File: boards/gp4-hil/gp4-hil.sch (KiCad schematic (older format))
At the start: 8 parts

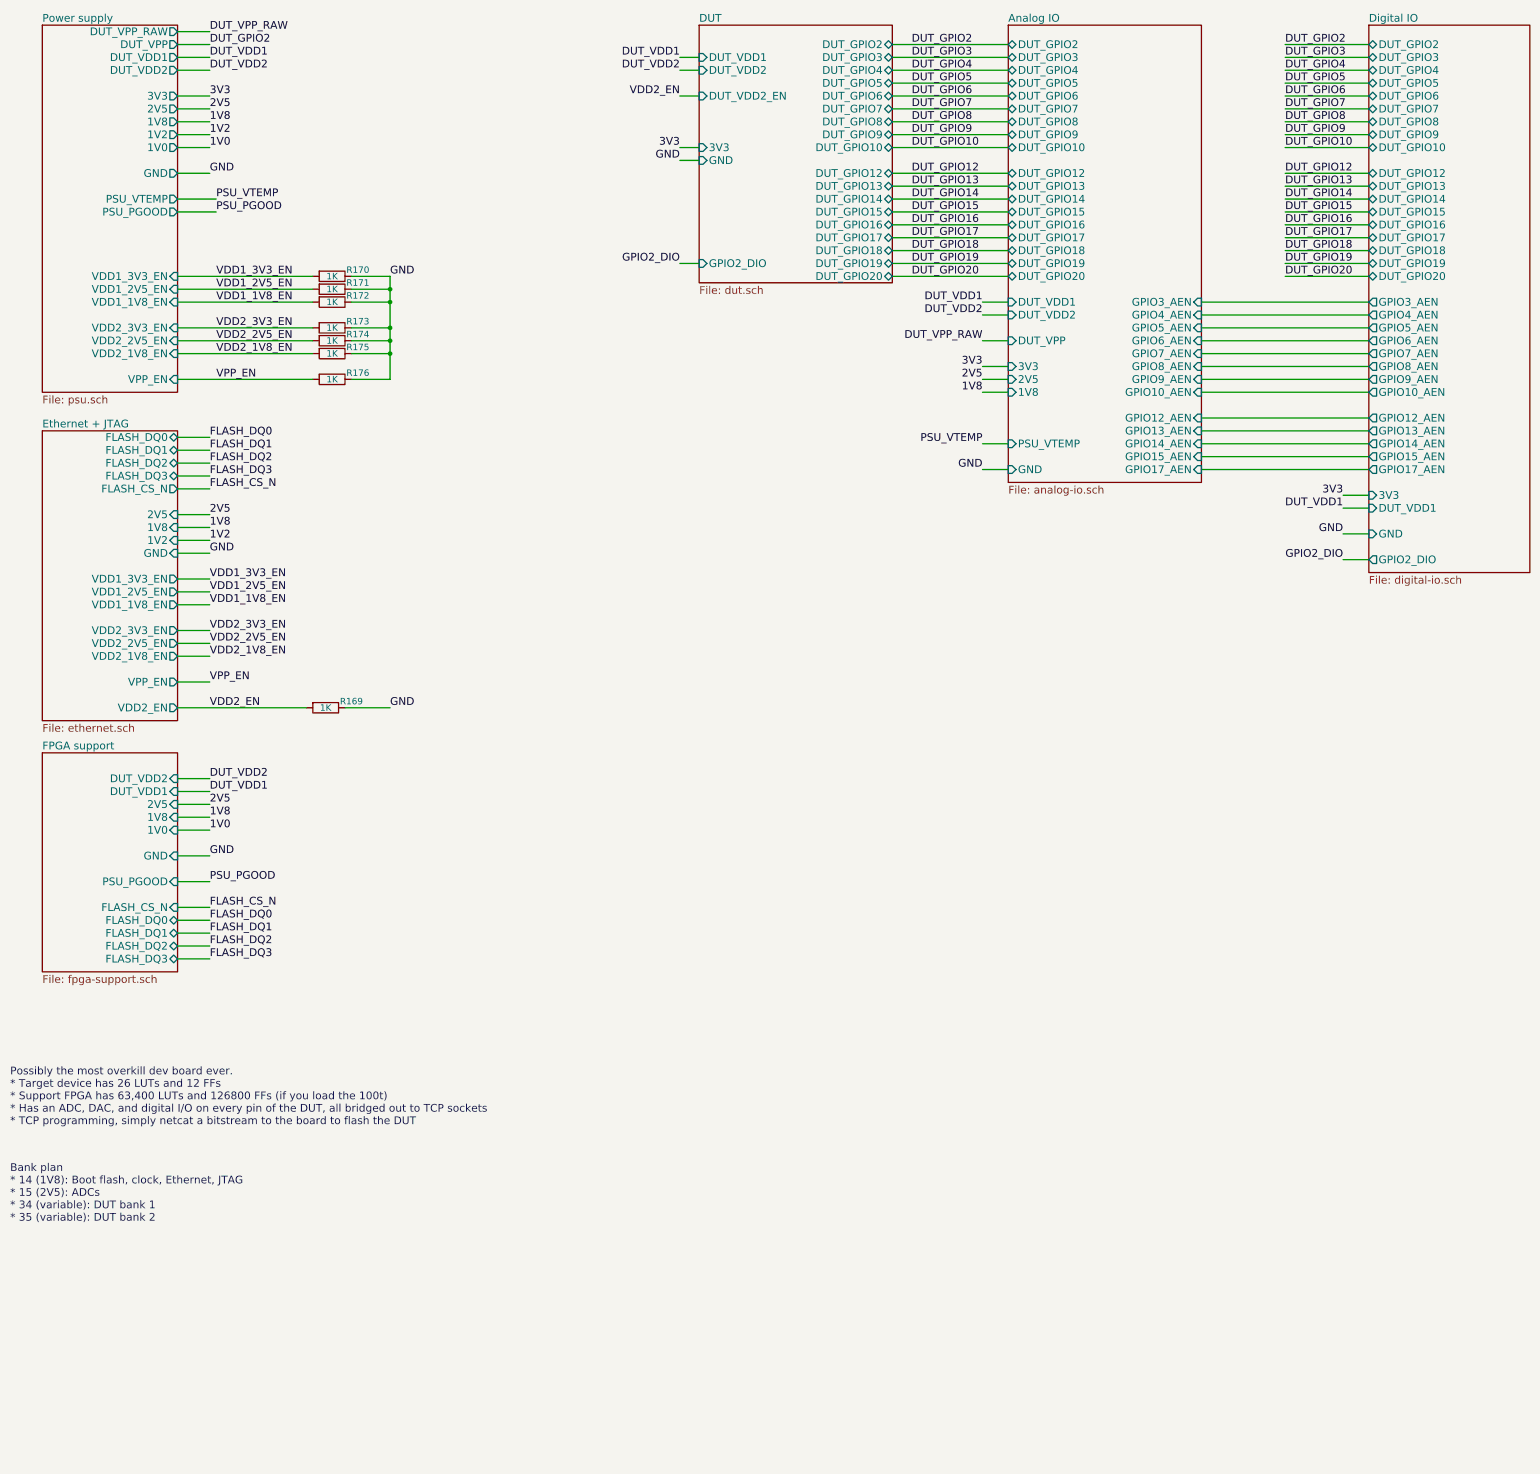
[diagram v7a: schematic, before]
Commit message: Added current monitoring shunts. Began design review
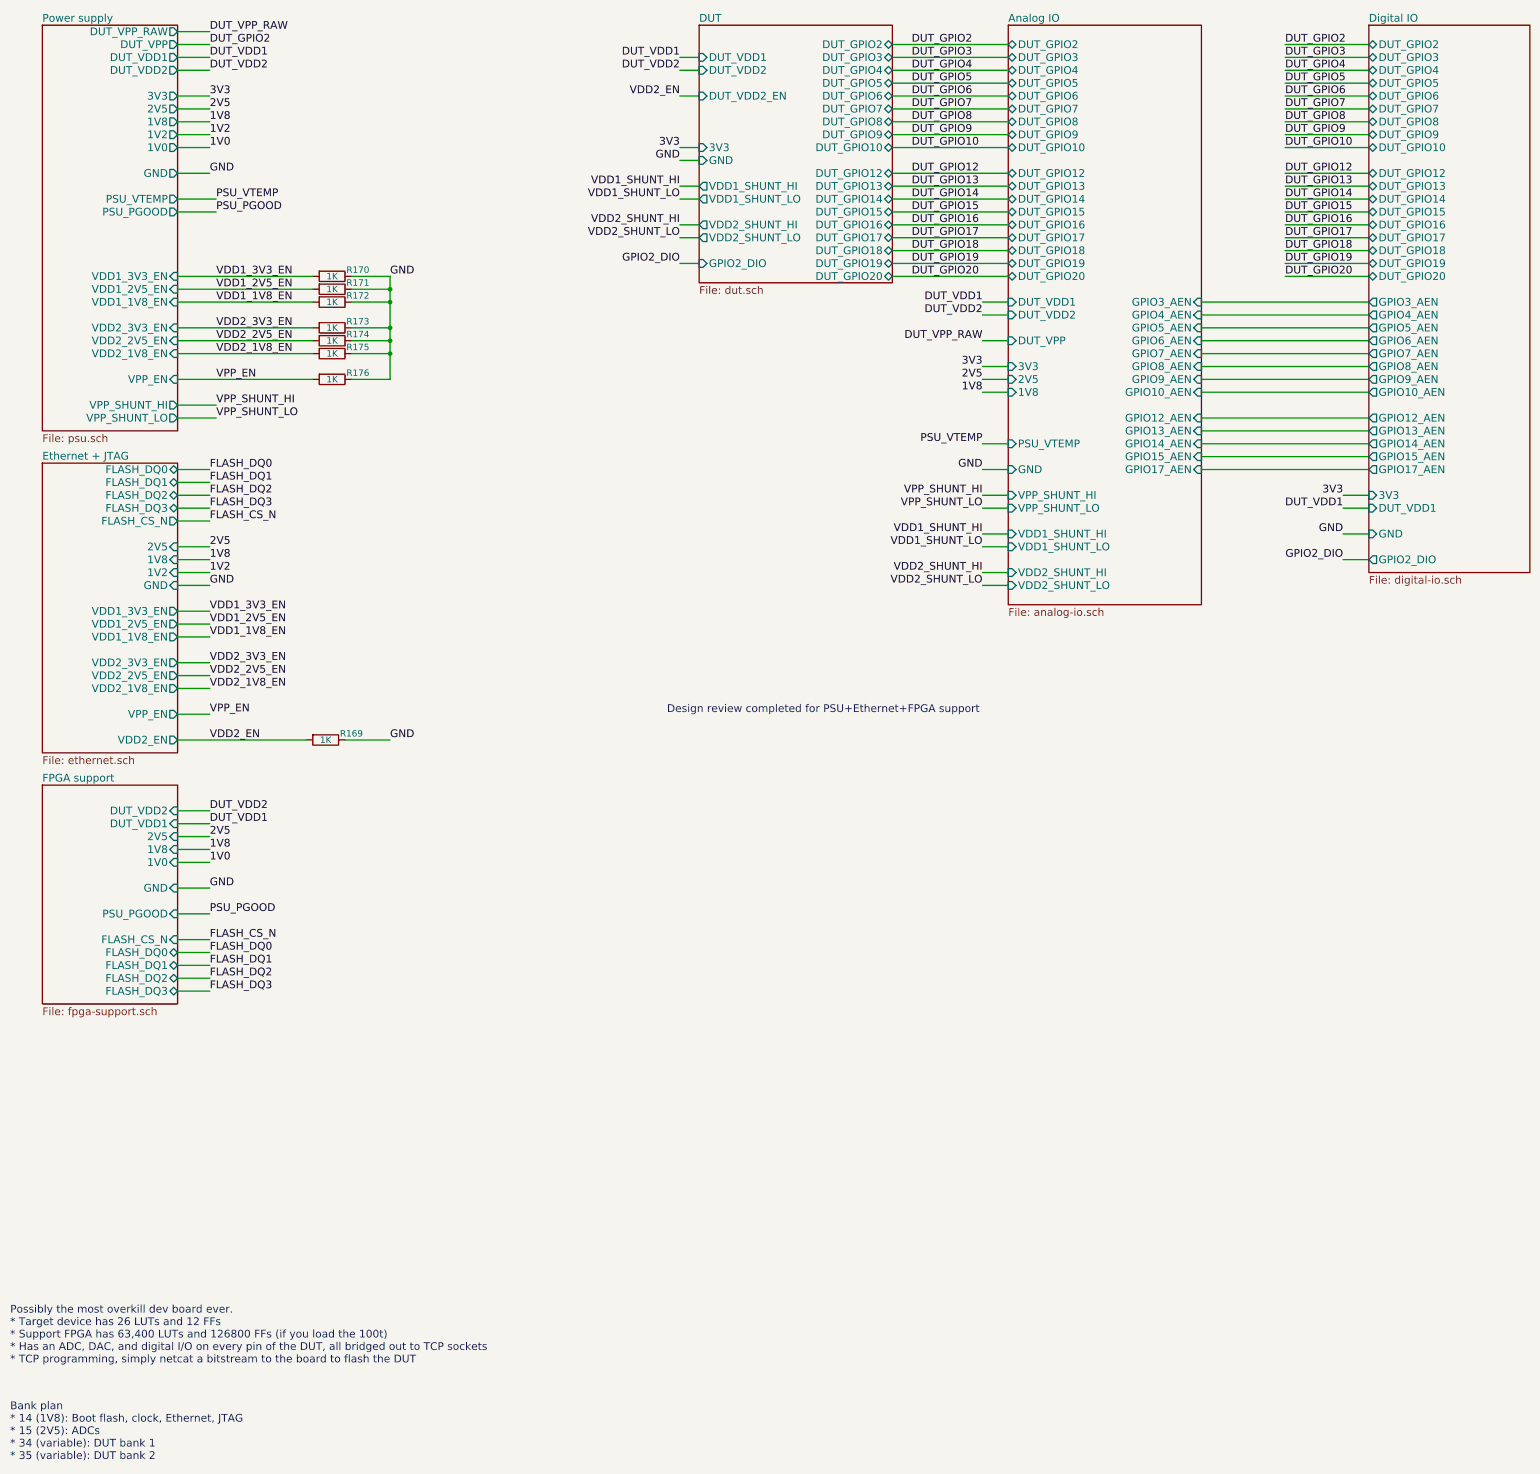
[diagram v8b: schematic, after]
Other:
- note added: "Design review completed for PSU+Ethernet+FPGA support"
- moved on the sheet: R169
